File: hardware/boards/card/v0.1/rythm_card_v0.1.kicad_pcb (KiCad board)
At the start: 6 copper layers, 50 x 30 mm, 7 parts, among them J1 USB_C_Receptacle, J2 USB_C_Receptacle_USB2.0_16P, U2 STM32H743VGHx

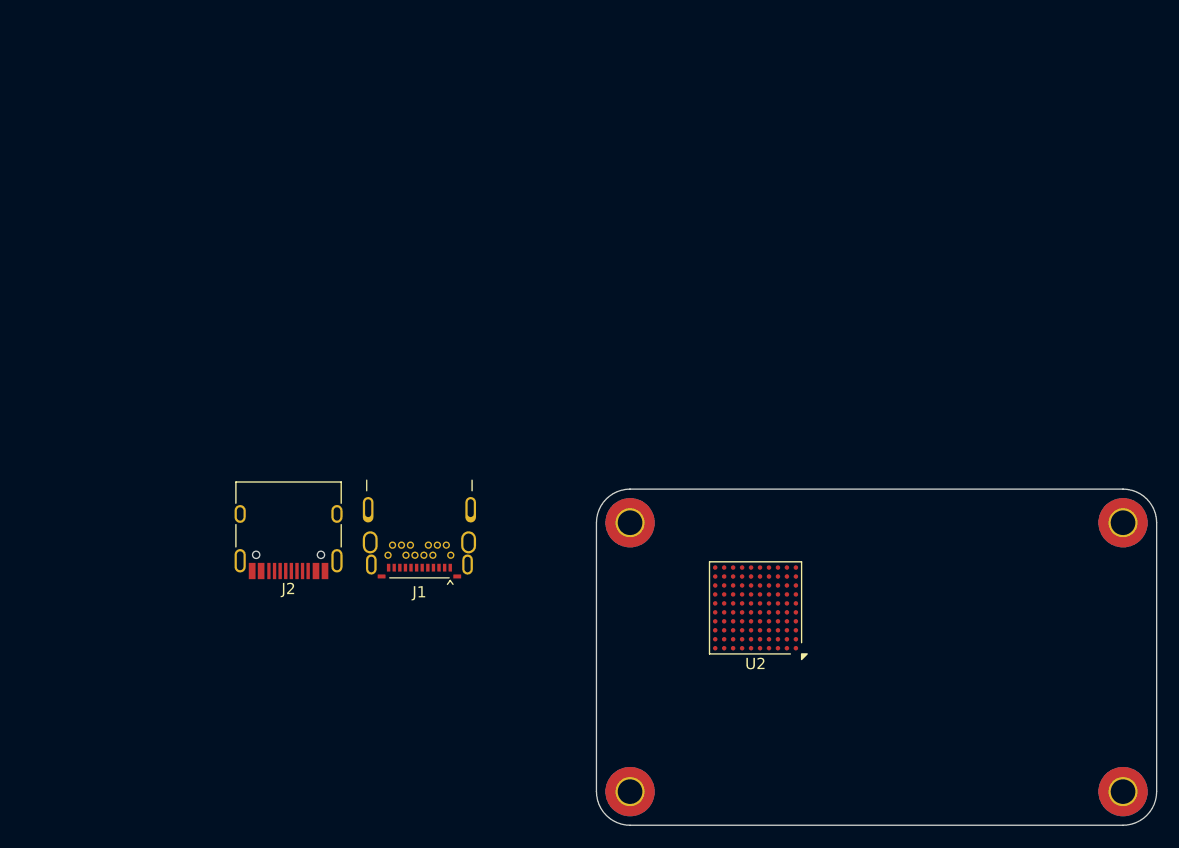
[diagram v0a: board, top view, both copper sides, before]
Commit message: testing routing layout on card board
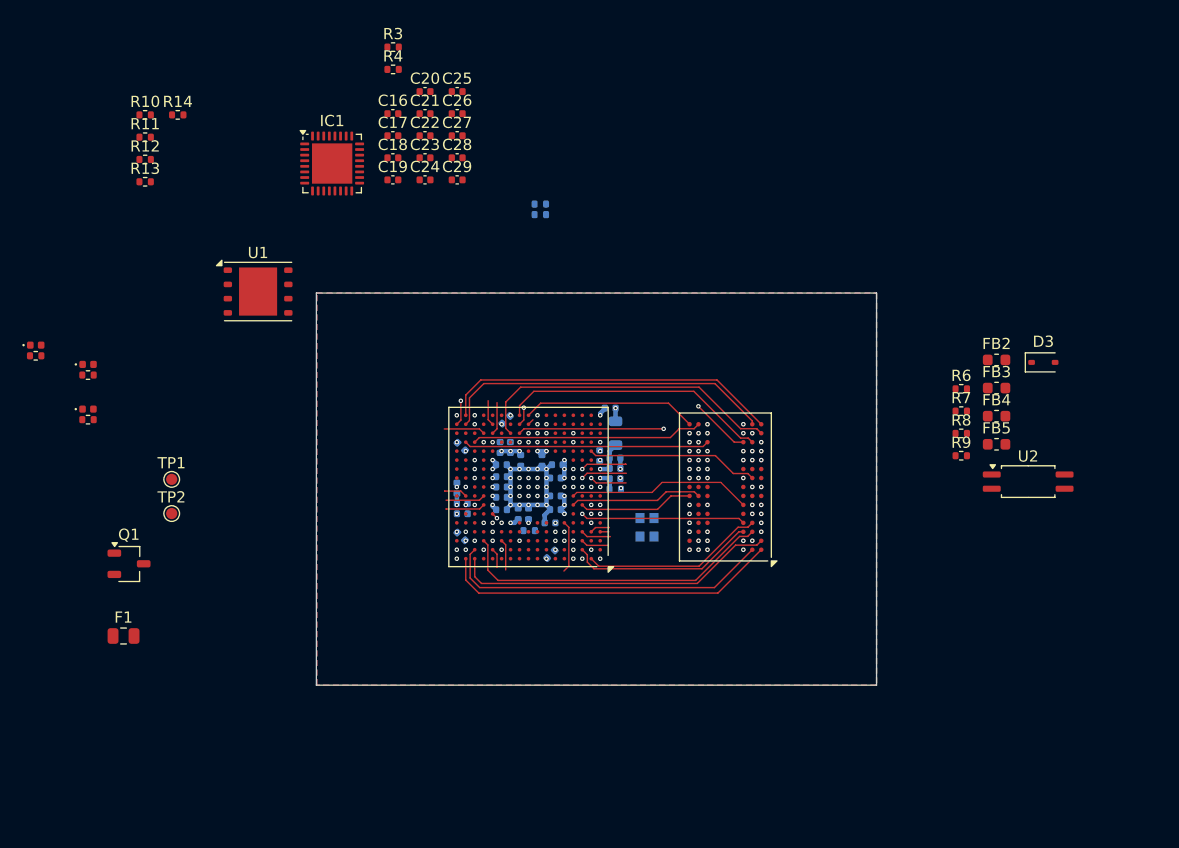
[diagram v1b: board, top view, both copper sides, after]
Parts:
- removed H1, H2, H3, H4: MountingHole_Pad, MountingHole:MountingHole_2.2mm_M2_Pad_TopBottom
- removed J1: USB_C_Receptacle, Connector_USB:USB_C_Receptacle_CNCTech_C-ARA1-AK51X
- removed J2: USB_C_Receptacle_USB2.0_16P, Connector_USB:USB_C_Receptacle_HRO_TYPE-C-31-M-12
- added C1: 2.2 uF <100 mΩ ESR, Capacitor_SMD:C_0402_1005Metric, B.Cu at (71.9, 73.8)
- added C15: R, Capacitor_SMD:C_0402_1005Metric, B.Cu at (80.3, 77.0)
- added C16: 4.7uF, Capacitor_SMD:C_0402_1005Metric, F.Cu at (61.8, 46.5)
- added C17: 4.7uF, Capacitor_SMD:C_0402_1005Metric, F.Cu at (61.8, 48.5)
- added C18: 4.7uF, Capacitor_SMD:C_0402_1005Metric, F.Cu at (61.8, 50.4)
- added C19: 4.7uF, Capacitor_SMD:C_0402_1005Metric, F.Cu at (61.8, 52.4)
- added C2: 2.2 uF <100 mΩ ESR, Capacitor_SMD:C_0402_1005Metric, B.Cu at (67.9, 84.2)
- added C20: 1uF, Capacitor_SMD:C_0402_1005Metric, F.Cu at (64.7, 44.5)
- added C21: 1uF, Capacitor_SMD:C_0402_1005Metric, F.Cu at (64.7, 46.5)
- added C22: 1uF, Capacitor_SMD:C_0402_1005Metric, F.Cu at (64.7, 48.5)
- added C23: 1uF, Capacitor_SMD:C_0402_1005Metric, F.Cu at (64.7, 50.4)
- added C24: 1uF, Capacitor_SMD:C_0402_1005Metric, F.Cu at (64.7, 52.4)
- added C25: 1uF, Capacitor_SMD:C_0402_1005Metric, F.Cu at (67.6, 44.5)
- added C26: 1uF, Capacitor_SMD:C_0402_1005Metric, F.Cu at (67.6, 46.5)
- added C27: 1uF, Capacitor_SMD:C_0402_1005Metric, F.Cu at (67.6, 48.5)
- added C28: 4.7uF, Capacitor_SMD:C_0402_1005Metric, F.Cu at (67.6, 50.4)
- added C29: 4.7uF, Capacitor_SMD:C_0402_1005Metric, F.Cu at (67.6, 52.4)
- added C3: 2.2 uF <100 mΩ ESR, Capacitor_SMD:C_0402_1005Metric, B.Cu at (75.9, 85.8)
- added C30: 10nF, Capacitor_SMD:C_0402_1005Metric, B.Cu at (81.7, 78.2)
- added C31: 1uF, Capacitor_SMD:C_0402_1005Metric, B.Cu at (81.7, 77.2)
- added C32: 1uF, Capacitor_SMD:C_0402_1005Metric, B.Cu at (81.2, 72.8)
- added C33: 100nF, Capacitor_SMD:C_0402_1005Metric, B.Cu at (81.7, 79.1)
- added C4: 1uF 600mΩ, Capacitor_SMD:C_0402_1005Metric, B.Cu at (68.0, 82.2)
- added C48: 100nF, Capacitor_SMD:C_0402_1005Metric, B.Cu at (71.4, 76.3)
- added C5: 100nF, Capacitor_SMD:C_0402_1005Metric, B.Cu at (68.0, 81.3)
- added C50: 100nF, Capacitor_SMD:C_0402_1005Metric, B.Cu at (71.5, 77.8)
- added C51: 100nF, Capacitor_SMD:C_0402_1005Metric, B.Cu at (71.5, 81.8)
- added C52: 100nF, Capacitor_SMD:C_0402_1005Metric, B.Cu at (76.5, 77.8)
- added C54: 100nF, Capacitor_SMD:C_0402_1005Metric, B.Cu at (72.3, 76.3)
- added C55: 100nF, Capacitor_SMD:C_0402_1005Metric, B.Cu at (71.5, 78.9)
- added C56: 100nF, Capacitor_SMD:C_0402_1005Metric, B.Cu at (73.9, 82.2)
- added C57: 100nF, Capacitor_SMD:C_0402_1005Metric, B.Cu at (71.5, 80.7)
- added C58: 100nF, Capacitor_SMD:C_0402_1005Metric, B.Cu at (76.3, 79.0)
- added C6: 1uF, Capacitor_SMD:C_0402_1005Metric, B.Cu at (67.5, 79.9)
- added C60: 100nF, Capacitor_SMD:C_0402_1005Metric, B.Cu at (67.9, 76.2)
- added C61: 100nF, Capacitor_SMD:C_0402_1005Metric, B.Cu at (73.2, 77.4)
- added C62: 100nF, Capacitor_SMD:C_0402_1005Metric, B.Cu at (75.9, 83.0)
- added C63: 100nF, Capacitor_SMD:C_0402_1005Metric, B.Cu at (71.5, 79.8)
- added C64: 100nF, Capacitor_SMD:C_0402_1005Metric, B.Cu at (76.3, 80.6)
- added C67: 100nF, Capacitor_SMD:C_0402_1005Metric, B.Cu at (75.1, 77.4)
- added C68: 100nF, Capacitor_SMD:C_0402_1005Metric, B.Cu at (73.0, 82.2)
- added C69: 10uF, Capacitor_SMD:C_0402_1005Metric, B.Cu at (76.3, 81.8)
- added D1: POWER, LED_SMD:LED_0402_1005Metric, F.Cu at (30.0, 67.2)
- added D2: STATUS, LED_SMD:LED_0402_1005Metric, F.Cu at (34.6, 68.9)
- added D3: 1N4148WS, Diode_SMD:D_SOD-323, F.Cu at (119.9, 68.7)
- added D4: STATUS2, LED_SMD:LED_0402_1005Metric, F.Cu at (34.6, 72.9)
- added F1: Polyfuse, Fuse:Fuse_0805_2012Metric, F.Cu at (37.8, 93.1)
- added FB1: 120R, Inductor_SMD:L_0805_2012Metric, B.Cu at (81.7, 75.0)
- added FB2: 1K @100MHz, Inductor_SMD:L_0603_1608Metric, F.Cu at (115.7, 68.5)
- added FB3: 1K @100MHz, Inductor_SMD:L_0603_1608Metric, F.Cu at (115.7, 71.0)
- added FB4: 1K @100MHz, Inductor_SMD:L_0603_1608Metric, F.Cu at (115.7, 73.5)
- added FB5: 1K @100MHz, Inductor_SMD:L_0603_1608Metric, F.Cu at (115.7, 76.0)
- added IC1: NAU88C22YG, Package_DFN_QFN:QFN-32-1EP_5x5mm_P0.5mm_EP3.6x3.6mm, F.Cu at (56.4, 50.9)
- added IC2: IS42S32160F-6BLI, Package_BGA:BGA-90_8.0x13.0mm_Layout2x3x15_P0.8mm, F.Cu at (91.5, 79.8)
- added Q1: PMV37EN22, Package_TO_SOT_SMD:TSOT-23, F.Cu at (38.3, 86.7)
- added R1: 4.7k, Resistor_SMD:R_0402_1005Metric, B.Cu at (75.0, 55.5)
- added R10: 10k, Resistor_SMD:R_0402_1005Metric, F.Cu at (39.7, 46.6)
- added R11: 10k, Resistor_SMD:R_0402_1005Metric, F.Cu at (39.7, 48.6)
- added R12: 10k, Resistor_SMD:R_0402_1005Metric, F.Cu at (39.7, 50.6)
- added R13: 10k, Resistor_SMD:R_0402_1005Metric, F.Cu at (39.7, 52.6)
- added R14: 10k, Resistor_SMD:R_0402_1005Metric, F.Cu at (42.6, 46.6)
- added R15: R, Resistor_SMD:R_0402_1005Metric, F.Cu at (34.6, 69.8)
- added R16: R, Resistor_SMD:R_0402_1005Metric, F.Cu at (29.9, 68.1)
- added R17: R, Resistor_SMD:R_0402_1005Metric, F.Cu at (34.6, 73.8)
- added R18: 10k, Resistor_SMD:R_0402_1005Metric, B.Cu at (74.0, 83.7)
- added R2: 4.7k, Resistor_SMD:R_0402_1005Metric, B.Cu at (75.0, 54.6)
- added R3: 2k2, Resistor_SMD:R_0402_1005Metric, F.Cu at (61.9, 40.5)
- added R4: 2k2, Resistor_SMD:R_0402_1005Metric, F.Cu at (61.9, 42.5)
- added R5: 10k, Resistor_SMD:R_0402_1005Metric, B.Cu at (81.7, 80.0)
- added R6: R, Resistor_SMD:R_0402_1005Metric, F.Cu at (112.6, 71.0)
- added R7: 220R, Resistor_SMD:R_0402_1005Metric, F.Cu at (112.6, 73.0)
- added R8: 10Ω 5% 0.25W, Resistor_SMD:R_0402_1005Metric, F.Cu at (112.6, 75.0)
- added R9: 33Ω 5% 0.5W, Resistor_SMD:R_0402_1005Metric, F.Cu at (112.6, 77.0)
- added TP1: GND, TestPoint:TestPoint_Pad_D1.0mm, F.Cu at (42.1, 79.1)
- added TP2: 3v3, TestPoint:TestPoint_Pad_D1.0mm, F.Cu at (42.1, 82.2)
- added U1: W25Q128JVP, Package_SON:WSON-8-1EP_6x5mm_P1.27mm_EP3.4x4.3mm, F.Cu at (49.8, 62.4)
- added U4: STM32H750XBHx, Package_BGA:TFBGA-265_14x14mm_Layout17x17_P0.8mm, F.Cu at (73.9, 79.8)
- added Y1: Crystal_GND24, Crystal:Crystal_SMD_Abracon_ABM10-4Pin_2.5x2.0mm, B.Cu at (84.5, 83.4)
- U2: value STM32H743VGHx -> LTV-217-G; footprint Package_BGA:TFBGA-100_8x8mm_Layout10x10_P0.8mm -> Package_SO:SOIC-4_4.55x2.6mm_P1.27mm
- moved U2 26.8 mm to (118.5, 79.3), turned to 0 degrees
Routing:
- net +3.3V: track 0.00 -> 35.9 mm, vias 0 -> 39
- net /FMC_D14: track 0.00 -> 30.6 mm, vias 0 -> 2
- net /FMC_D13: track 0.00 -> 30.4 mm
- net /FMC_D24: track 0.00 -> 30.4 mm
- net /FMC_D15: track 0.00 -> 29.9 mm
- net /FMC_D26: track 0.00 -> 29.6 mm
- net /FMC_D25: track 0.00 -> 29.0 mm
- net /FMC_D22: track 0.00 -> 28.8 mm, vias 0 -> 2
- net /FMC_D27: track 0.00 -> 28.6 mm
- net /FMC_D12: track 0.00 -> 28.0 mm
- net /FMC_D21: track 0.00 -> 26.2 mm, vias 0 -> 2
- net /FMC_D10: track 0.00 -> 25.1 mm, vias 0 -> 2
- net /FMC_D11: track 0.00 -> 24.0 mm
- net /FMC_D23: track 0.00 -> 22.9 mm, vias 0 -> 2
- net GND: track 0.00 -> 22.2 mm, vias 0 -> 65
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- added copper zone on In2.Cu, net +3.3V
- added copper zone on B.Cu, net GND
- added copper zone on F.Cu, net GND
- added copper zone on In1.Cu, net GND
- added copper zone on In4.Cu, net GND
- added copper zone on In6.Cu, net GND
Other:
- board size 50 x 30 mm -> 50 x 35 mm
- copper layers 6 -> 8
